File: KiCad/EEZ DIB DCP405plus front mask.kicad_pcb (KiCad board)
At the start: 2 copper layers, 35 x 111.5 mm, 1 part

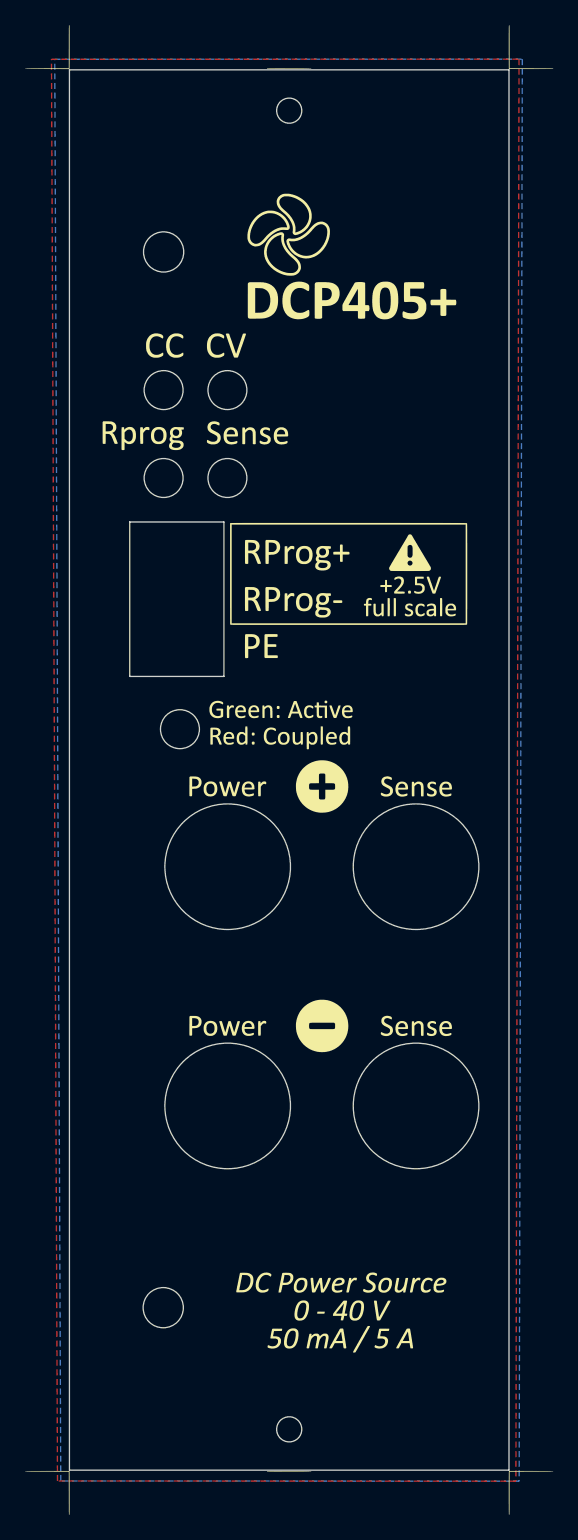
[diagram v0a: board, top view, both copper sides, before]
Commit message: r4B3 version: OE fixed, new LEDs for remote programming
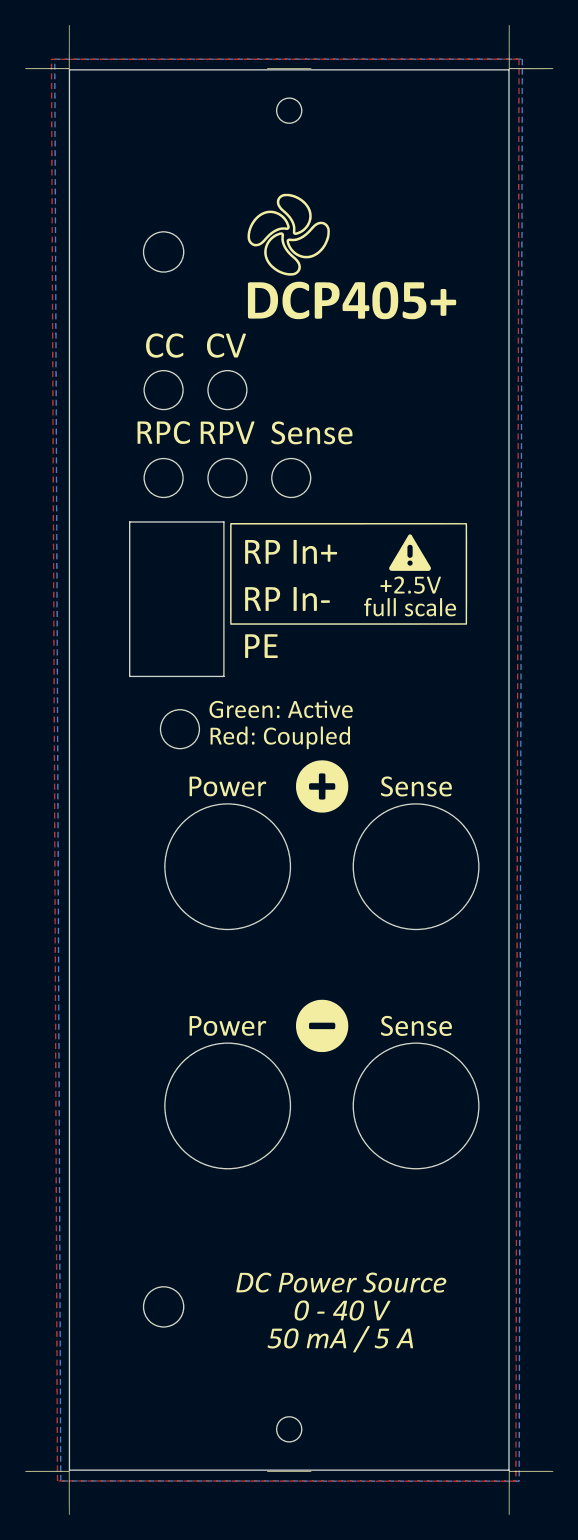
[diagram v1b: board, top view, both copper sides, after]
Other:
- outline, holes or cut-outs redrawn

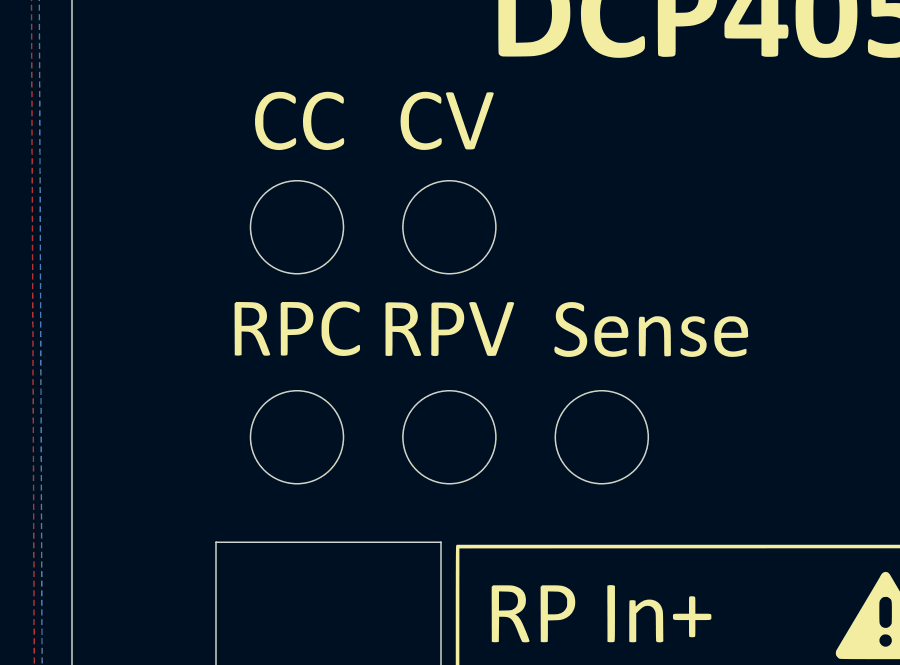
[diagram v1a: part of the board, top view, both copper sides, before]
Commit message: Front mask gerbers and dxf update
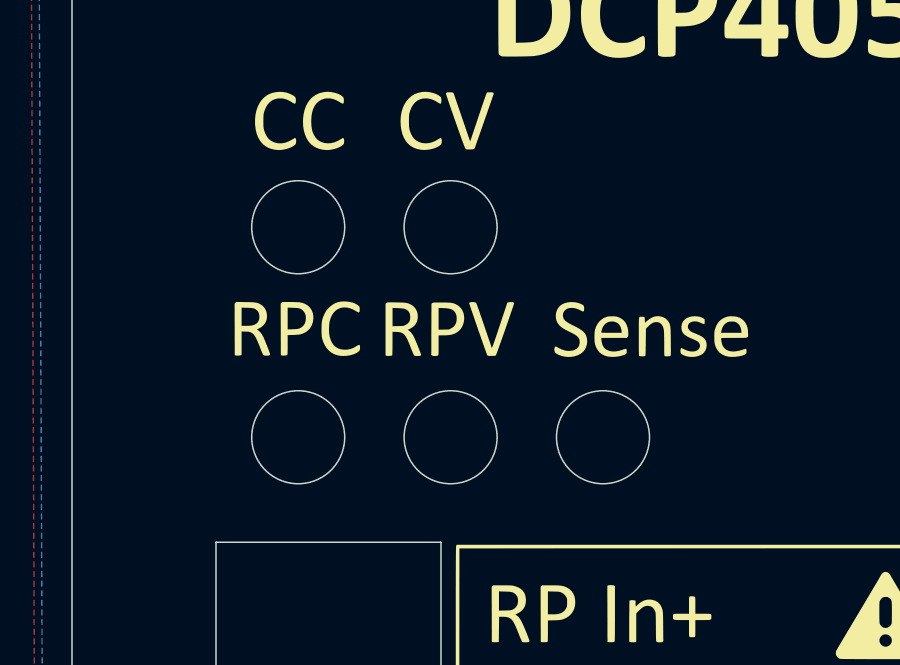
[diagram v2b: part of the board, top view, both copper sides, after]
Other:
- outline, holes or cut-outs redrawn
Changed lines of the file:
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@@
 	)
 	(gr_circle
-		(center 148 71)
-		(end 149.55 71)
+		(center 148.04 71)
+		(end 149.59 71)
 		(stroke
 			(width 0.05)
@@
 	)
 	(gr_circle
-		(center 153.08 64)
-		(end 154.63 64)
+		(center 153.12 64)
+		(end 154.67 64)
 		(stroke
 			(width 0.05)
@@
 	)
 	(gr_circle
-		(center 158.16 71)
-		(end 159.71 71)
+		(center 158.2 71)
+		(end 159.75 71)
 		(stroke
 			(width 0.05)
@@
 	)
 	(gr_circle
-		(center 153.08 71)
-		(end 154.63 71)
+		(center 153.12 71)
+		(end 154.67 71)
 		(stroke
 			(width 0.05)
@@
 	)
 	(gr_circle
-		(center 148 64)
-		(end 149.55 64)
+		(center 148.04 64)
+		(end 149.59 64)
 		(stroke
 			(width 0.05)
@@
 	)
 	(dimension
-		(type center)
-		(layer "User.1")
-		(pts
-			(xy 147.999999 64.05) (xy 146.449999 64.05)
-		)
-		(style
-			(thickness 0.1)
-			(arrow_length 1.27)
-			(text_position_mode 0)
-			(extension_offset 0.5)
-			(keep_text_aligned yes)
-		)
-	)
-	(dimension
 		(type orthogonal)
 		(layer "User.1")
@@
 		(layer "User.1")
 		(pts
-			(xy 140.5 150) (xy 140.47 38.562499)
+			(xy 140.5 150) (xy 140.5 38.5)
 		)
 		(height -28.82)
@@
 			(keep_text_aligned yes)
 		)
-		(gr_text "111,4 mm"
-			(at 110.53 94.281249 90)
+		(gr_text "111,5 mm"
+			(at 110.53 94.25 90)
 			(layer "User.1")
 			(effects
@@
 		(layer "User.1")
 		(pts
+			(xy 158 41.75) (xy 158 146.75)
+		)
+		(height 27.5)
+		(orientation 1)
+		(format
+			(prefix "")
+			(suffix "")
+			(units 3)
+			(units_format 0)
+			(precision 4)
+			(suppress_zeroes yes)
+		)
+		(style
+			(thickness 0.1)
+			(arrow_length 1.27)
+			(text_position_mode 0)
+			(arrow_direction outward)
+			(extension_height 0.58642)
+			(extension_offset 0.5)
+			(keep_text_aligned yes)
+		)
+		(gr_text "105"
+			(at 184.35 94.25 90)
+			(layer "User.1")
+			(effects
+				(font
+					(size 1 1)
+					(thickness 0.15)
+				)
+			)
+		)
+	)
+	(dimension
+		(type orthogonal)
+		(layer "User.1")
+		(pts
 			(xy 140.5 146.3) (xy 158.01 146.3)
 		)
@@
 		(layer "User.1")
 		(pts
+			(xy 114.51 53.05) (xy 114.51 38.55)
+		)
+		(height 0)
+		(orientation 1)
+		(format
+			(prefix "")
+			(suffix "")
+			(units 3)
+			(units_format 0)
+			(precision 4)
+			(suppress_zeroes yes)
+		)
+		(style
+			(thickness 0.1)
+			(arrow_length 1.27)
+			(text_position_mode 0)
+			(arrow_direction outward)
+			(extension_height 0.58642)
+			(extension_offset 0.5)
+			(keep_text_aligned yes)
+		)
+		(gr_text "14,5"
+			(at 113.36 45.8 90)
+			(layer "User.1")
+			(effects
+				(font
+					(size 1 1)
+					(thickness 0.15)
+				)
+			)
+		)
+	)
+	(dimension
+		(type orthogonal)
+		(layer "User.1")
+		(pts
 			(xy 140.5 150) (xy 146 86.8)
 		)
@@
 		(layer "User.1")
 		(pts
-			(xy 148 64.05) (xy 140.48 65.492499)
+			(xy 153.12 71) (xy 158.2 71)
+		)
+		(height 3.07)
+		(orientation 0)
+		(format
+			(prefix "")
+			(suffix "")
+			(units 3)
+			(units_format 0)
+			(precision 4)
+			(suppress_zeroes yes)
+		)
+		(style
+			(thickness 0.1)
+			(arrow_length 1.27)
+			(text_position_mode 0)
+			(arrow_direction outward)
+			(extension_height 0.58642)
+			(extension_offset 0.5)
+			(keep_text_aligned yes)
+		)
+		(gr_text "5,08"
+			(at 155.66 72.92 0)
+			(layer "User.1")
+			(effects
+				(font
+					(size 1 1)
+					(thickness 0.15)
+				)
+			)
+		)
+	)
+	(dimension
+		(type orthogonal)
+		(layer "User.1")
+		(pts
+			(xy 147.999999 64.05) (xy 140.5 65.48)
 		)
 		(height 3.562499)
@@
 		)
 		(gr_text "7,5 mm"
-			(at 144.24 66.462499 0)
+			(at 144.249999 66.462499 0)
 			(layer "User.1")
 			(effects
@@
 		(layer "User.1")
 		(pts
+			(xy 148.04 64) (xy 153.12 64)
+		)
+		(height -2.72)
+		(orientation 0)
+		(format
+			(prefix "")
+			(suffix "")
+			(units 3)
+			(units_format 0)
+			(precision 4)
+			(suppress_zeroes yes)
+		)
+		(style
+			(thickness 0.1)
+			(arrow_length 1.27)
+			(text_position_mode 0)
+			(arrow_direction outward)
+			(extension_height 0.58642)
+			(extension_offset 0.5)
+			(keep_text_aligned yes)
+		)
+		(gr_text "5,08"
+			(at 150.58 60.13 0)
+			(layer "User.1")
+			(effects
+				(font
+					(size 1 1)
+					(thickness 0.15)
+				)
+			)
+		)
+	)
+	(dimension
+		(type orthogonal)
+		(layer "User.1")
+		(pts
 			(xy 140.48 137.05) (xy 148 137.05)
 		)
@@
 		(layer "User.1")
 		(pts
-			(xy 148 64.05) (xy 153 64.05)
-		)
-		(height -4.017501)
-		(orientation 0)
-		(format
-			(prefix "")
-			(suffix "")
-			(units 3)
-			(units_format 1)
-			(precision 1)
-		)
-		(style
-			(thickness 0.1)
-			(arrow_length 1.27)
-			(text_position_mode 0)
-			(arrow_direction outward)
-			(extension_height 0.58642)
-			(extension_offset 0.5)
-			(keep_text_aligned yes)
-		)
-		(gr_text "5,0 mm"
-			(at 150.5 58.882499 0)
-			(layer "User.1")
-			(effects
-				(font
-					(size 1 1)
-					(thickness 0.15)
-				)
-			)
-		)
-	)
-	(dimension
-		(type orthogonal)
-		(layer "User.1")
-		(pts
 			(xy 140.5 150) (xy 148 71.05)
 		)
@@
 		(layer "User.2")
 		(pts
-			(xy 147.999999 64.05) (xy 145.5 64.05)
-		)
-		(height -6.55)
-		(orientation 0)
-		(format
-			(prefix "")
-			(suffix "")
-			(units 3)
-			(units_format 0)
-			(precision 4)
-			(suppress_zeroes yes)
-		)
-		(style
-			(thickness 0.1)
-			(arrow_length 1.27)
-			(text_position_mode 0)
-			(arrow_direction outward)
-			(extension_height 0.58642)
-			(extension_offset 0.5)
-			(keep_text_aligned yes)
-		)
-		(gr_text "2,5"
-			(at 146.749999 56.35 0)
+			(xy 158 146.75) (xy 144.7 143.7)
+		)
+		(height 10.31)
+		(orientation 0)
+		(format
+			(prefix "")
+			(suffix "")
+			(units 3)
+			(units_format 0)
+			(precision 3)
+			(suppress_zeroes yes)
+		)
+		(style
+			(thickness 0.05)
+			(arrow_length 1.27)
+			(text_position_mode 0)
+			(arrow_direction outward)
+			(extension_height 0.58642)
+			(extension_offset 0.5)
+			(keep_text_aligned yes)
+		)
+		(gr_text "13,3"
+			(at 151.35 155.91 0)
 			(layer "User.2")
 			(effects
